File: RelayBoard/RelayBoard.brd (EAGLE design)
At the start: 139.1 x 115.2 mm, 254 parts, among them IC1 MCP2551/SN RSC 402-904, J1 JTAG_ARM_10PIN, J4 JTAG_ARM_10PIN, U1 CD74HC4067SM96, U10 INA219AIDCNR, U11 INA219AIDCNR, U12 INA219AIDCNR, U13 FT230XQ, U14 ADUM1201ARZ, U16 TL1963AKTTR., U2 TL1963AKTTR., U3 CD74HC4067SM96, U4 CD74HC4067SM96, U5 CD74HC4067SM96, U6 TL1963AKTTR., U8 TM4C1294NCPDT, U9 INA219AIDCNR, X1 A1944-50, X2 A1944-50, X3 A1944-50, X4 A1944-50, Y3 NX3225GA, Y4 CRYATL_32K_SMD

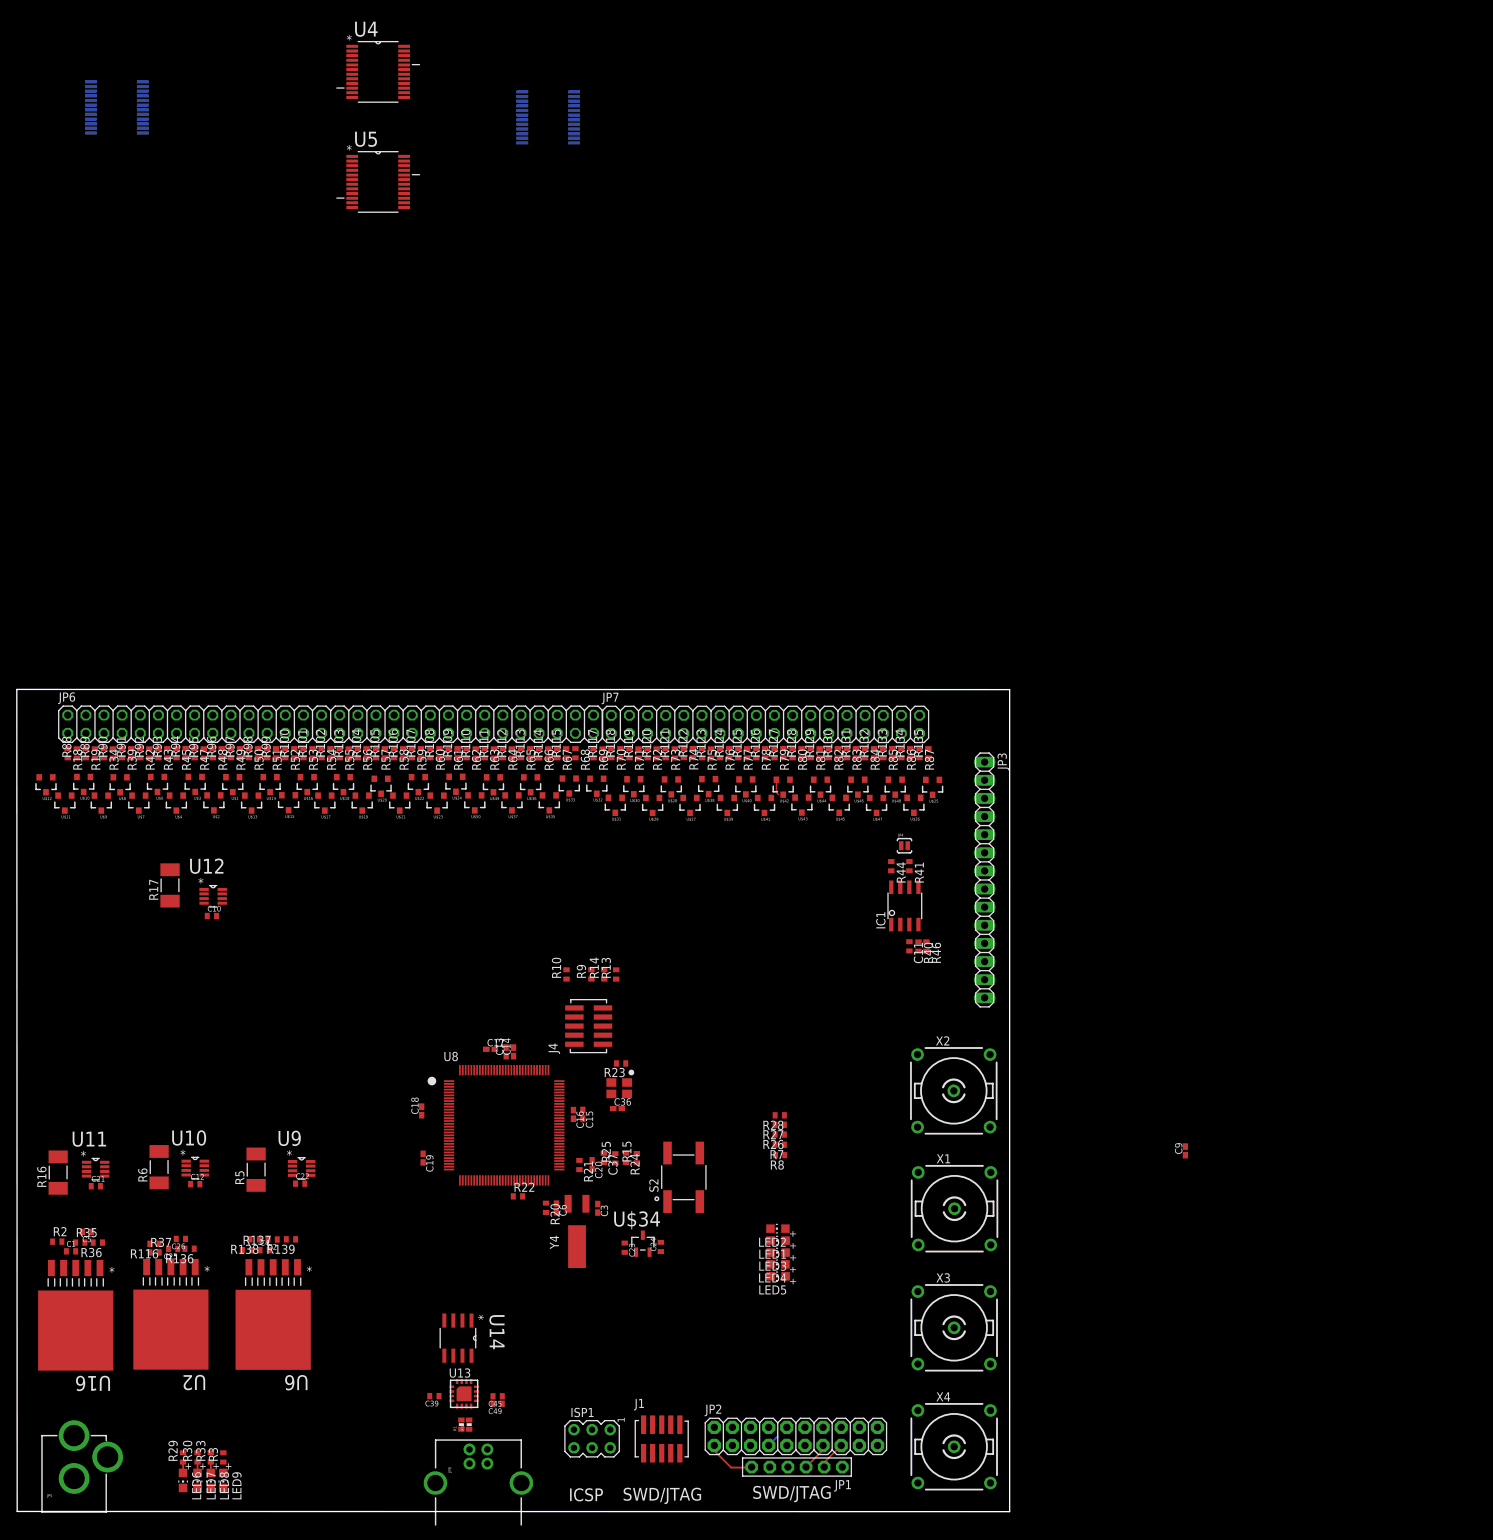
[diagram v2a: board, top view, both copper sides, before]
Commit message: layout done
Add: - binding posts with 19.05 mm spacing
         - top/bottom  VCC/GND plane
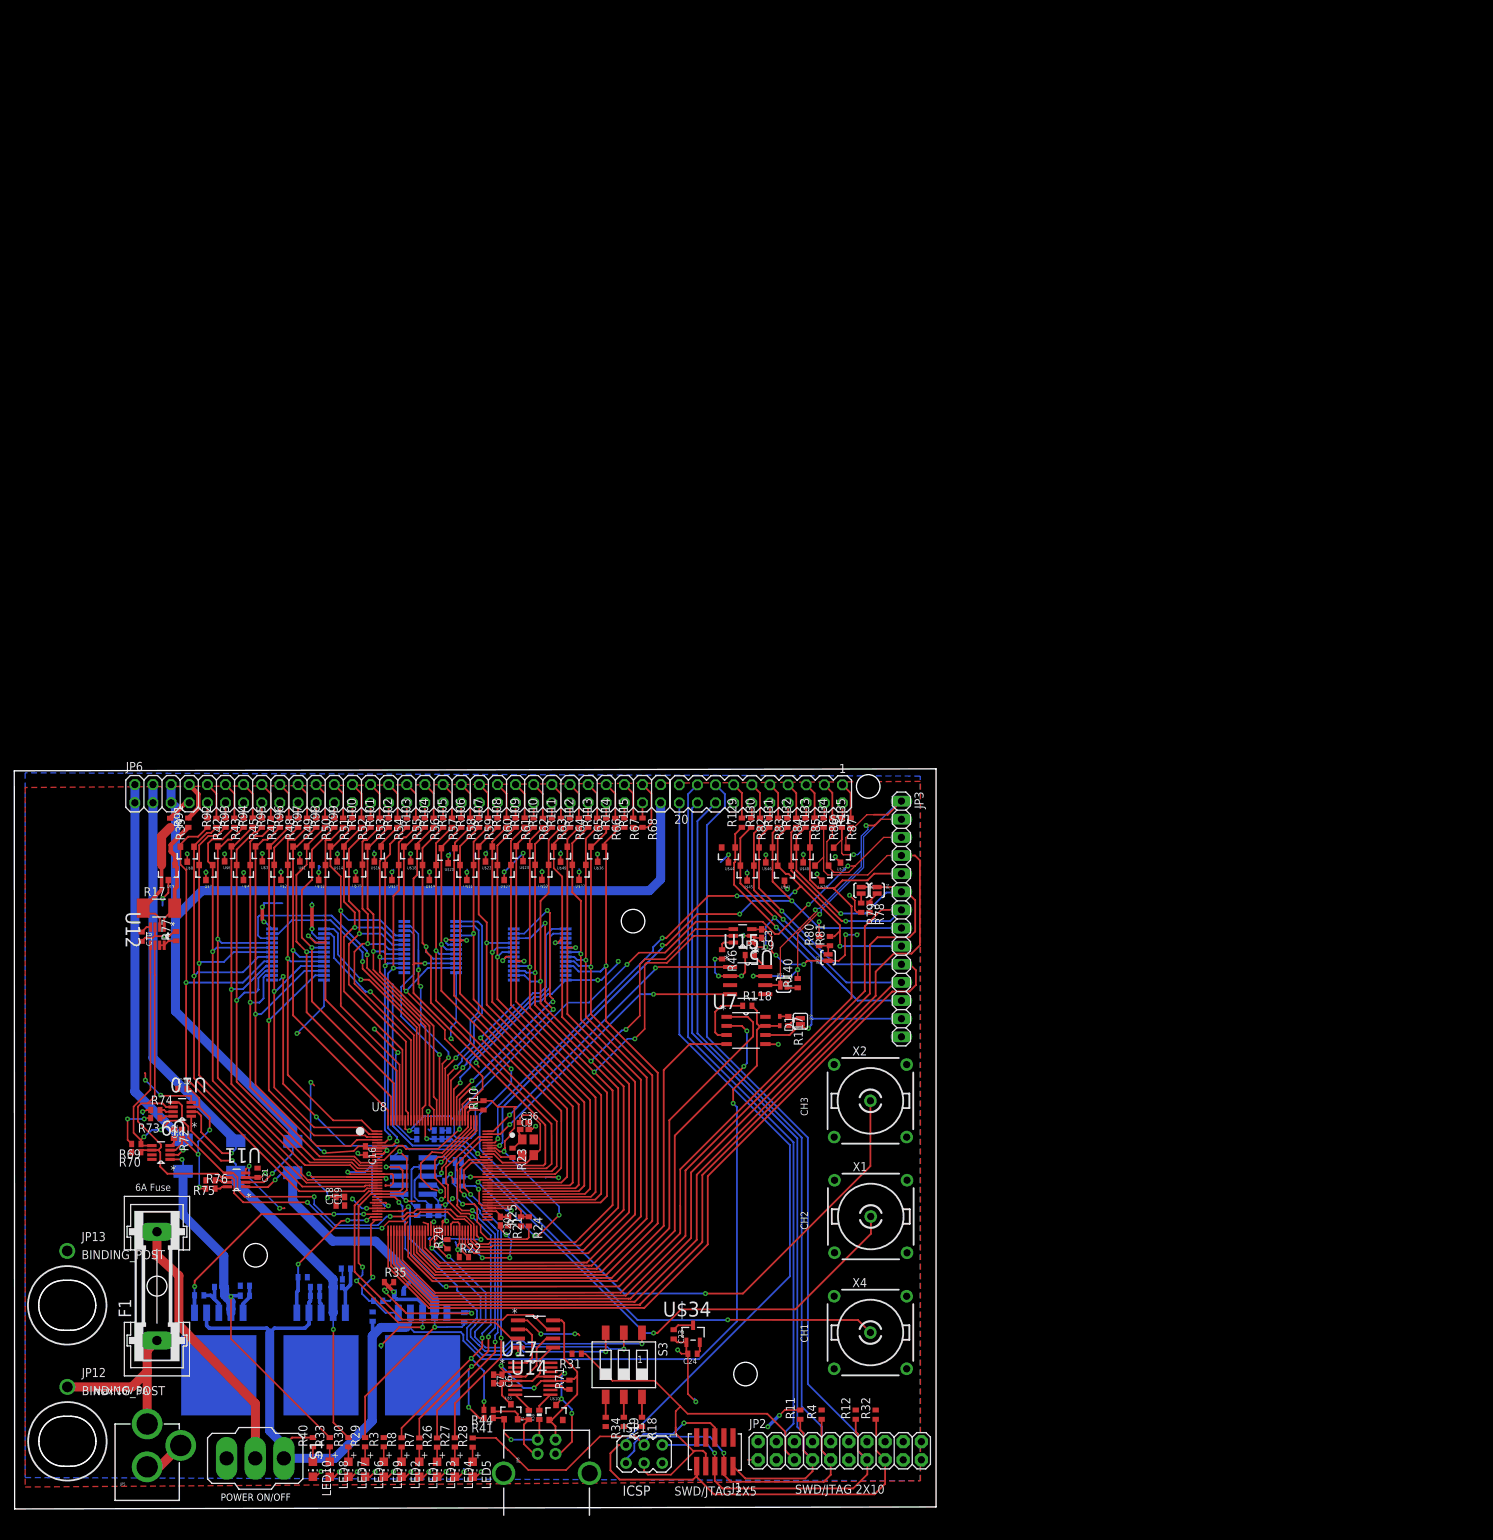
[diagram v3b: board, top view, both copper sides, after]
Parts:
- removed C11: 100nF, eagle-ltspice:C0402
- removed C39, C45: 0.1uF, rcl:C0402
- removed C49: 10uF, rcl:C0402
- removed IC1: MCP2551/SN RSC 402-904, microchip-dspic:SO08
- removed R120, R121, R122, R123, R124, R125, R126, R127, R128, R88, R89, R90: 200R, resistor:R0402
- removed S2: SWITCH_TACTILE, MRDT-UserInput:SWITCH_6MM_6MM_TE_CON_SMD
- removed U$11, U$12, U$27, U$28, U$29, U$30, U$31, U$32, U$33, U$35, U$38, U$39, U$40, U$41, U$42, U$43: zener_3.3V, SparkFun-DiscreteSemi:SOT23-3
- removed U13: FT230XQ, ftdichip:QFN16
- removed X3: A1944-50, con-coax:A1944
- removed Y4: CRYATL_32K_SMD, MRDT-Passives:CRYSTAL_32K_SMD
- added C7: 10uF, rcl:C0402K
- added D1: (no value), diode:SOD523
- added F1: (no value), fuse:GSH15
- added JP10: DUT_CS_MASTER, SparkFun-Retired:SJ_2S-NO
- added JP11: (no value), SparkFun:SJ_2S-NO
- added JP12, JP13: BINDING_POST, SparkFun-Connectors:BINDING_POST
- added JP9: (no value), SparkFun-Retired:SJ_2S
- added LED10: (no value), JDT-1800_smahed:CHIP-LED0805
- added R11, R12, R31, R32, R4: 4k7, resistor:R0402
- added R140: 120, resistor:R0402
- added S1: (no value), switch:320-916
- added S3: SWS003, smd-special:SMS-003
- added STANDOFF1, STANDOFF2, STANDOFF5, STANDOFF6: STAND-OFF, SparkFun-Electromechanical:STAND-OFF
- added SV1: (no value), con-lstb:MA10-2
- added U$5: zener_3.3V, SparkFun-DiscreteSemi:SOT23-3
- added U15: SN65HVD230D, sn65hvd23x:SOIC127P600X175-8N
- added U17: FT230XS, FT230XS:SOP63P600X175-16N
- added U7: MCP2003-E/SN, MCP2003-E_SN:SOIC127P600X175-8N
- C3, C6: value 12pF -> 0.1uF
- JP1: value (none) -> RESET; device JDT-1800_smahed:1X06-BIG -> SparkFun-Retired:SJ_2S-NO
- JP4: value (none) -> DUT_CS_MASTER; device SparkFun:SJ_2S-NO -> SparkFun-Retired:SJ_2S-NO
- JP7: value (none) -> DUT_CS_RecieveAllMSG; device pinhead:2X18 -> SparkFun-Retired:SJ_2S-NO
- R117: value 200R -> 1k
- R118, R119, R72, R73, R74, R75, R76, R77: value 200R -> 4k7
- R136, R139, R36: value (none) -> 4k7
- R18, R19, R34, R69, R70, R71, R78, R79, R80, R81: value 200R -> 4.7k
- R40: value 10k -> (none)
- R41: value 120 -> 0R
- R44: value 4k7 -> 0R
- R46: value 18k -> 4.7k
- U5: value CD74HC4067SM96 -> MCP4725A0T-E/CH; device MUX:SOP65P780X200-24N -> MCP4725:SOT95P270X145-6N
- moved U3 132.6 mm to (73.6, 77.9), turned to 180 degrees
- moved R18 123.5 mm to (87.9, 12.4)
- moved U4 122.8 mm to (58.2, 78.9), flipped to the bottom, turned to 180 degrees
- moved U1 122.4 mm to (39.7, 77.9), turned to 180 degrees
- moved R19 120.2 mm to (85.3, 12.4)
- moved U5 117.3 mm to (102.0, 80.5), turned to 180 degrees
- moved R34 117.1 mm to (82.8, 12.4)
- moved U$10 110.2 mm to (75.8, 13.7), turned to 0 degrees
- moved R40 109.6 mm to (41.8, 9.58), turned to 90 degrees
- moved R41 97.2 mm to (66.4, 13.0), turned to 180 degrees
- moved R44 94.8 mm to (66.4, 14.1), turned to 180 degrees
- moved R76 93.9 mm to (27.4, 45.1), turned to 0 degrees
- moved C9 92.6 mm to (71.4, 53.4), turned to 0 degrees
- moved R75 91.2 mm to (27.4, 46.3), turned to 180 degrees
- moved R74 89.3 mm to (19.7, 56.1), turned to 0 degrees
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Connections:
- removed net 5VSUPPLY: JP2.19
- removed net CAN_N: IC1.6, JP3.2, R41.2
- removed net CAN_P: IC1.7, JP3.1, JP4.1
- removed net CS: JP3.6
- removed net DUT_SH_-: R17.1, U12.2
- removed net EN0LED0: U8.P$42
- removed net EN0LED1: U8.P$46
- removed net EN0RXI_N: U8.P$53
- removed net EN0RXI_P: U8.P$54
- removed net EN0TXO_N: U8.P$56
- removed net EN0TXO_P: U8.P$57
- removed net LIN: JP3.13
- removed net M3S0: U5.10
- removed net M3S1: U5.11
- removed net M3S2: U5.14
- removed net M3S3: U5.13
- removed net MISO: JP3.4
- removed net MOSI: JP3.7
- removed net N$111: JP6.60, R117.2
- removed net N$113: R87.2, U$25.2
- removed net N$114: R88.1, U$12.1
- removed net N$115: R89.1, U$11.1
- removed net N$116: R19.2, U$11.2
- removed net N$117: R90.1, U$10.1
- removed net N$118: R34.2, U$10.2
- removed net N$119: R91.1, U$9.1
- removed net N$120: R39.2, U$9.2
- removed net N$121: R92.1, U$8.1
- removed net N$122: R42.2, U$8.2
- removed net N$123: R43.2, U$7.2
- removed net N$124: R93.1, U$7.1
- removed net N$125: R94.1, U$6.1
- removed net N$126: R45.2, U$6.2
- removed net N$127: R47.2, U$4.2
- removed net N$128: R95.1, U$4.1
- removed net N$129: R96.1, U$3.1
- removed net N$130: R48.2, U$3.2
- removed net N$131: R97.1, U$2.1
- removed net N$132: R49.2, U$2.2
- removed net N$133: R50.2, U$1.2
- removed net N$134: R98.1, U$1.1
- removed net N$135: R99.1, U$13.1
- removed net N$136: R51.2, U$13.2
- removed net N$137: R52.2, U$14.2
- removed net N$138: R100.1, U$14.1
- removed net N$139: R101.1, U$15.1
- removed net N$140: R53.2, U$15.2
- removed net N$141: R54.2, U$16.2
- removed net N$142: R102.1, U$16.1
- removed net N$143: R55.2, U$17.2
- removed net N$144: R103.1, U$17.1
- removed net N$145: R104.1, U$18.1
- removed net N$146: R56.2, U$18.2
- removed net N$147: R105.1, U$19.1
- removed net N$148: R57.2, U$19.2
- removed net N$149: R106.1, U$20.1
- removed net N$150: R58.2, U$20.2
- removed net N$151: R59.2, U$21.2
- removed net N$152: R107.1, U$21.1
- removed net N$157: R135.1, U$25.1
- removed net N$159: C39.2, U13.8
- removed net N$160: R134.1, U$26.1
- removed net N$161: R86.2, U$26.2
- removed net N$162: R85.2, U$48.2
- removed net N$163: R133.1, U$48.1
- removed net N$164: R84.2, U$47.2
- removed net N$165: R83.2, U$46.2
- removed net N$166: R82.2, U$45.2
- removed net N$167: R81.2, U$44.2
- removed net N$168: R80.2, U$43.2
- removed net N$169: R79.2, U$42.2
- removed net N$170: R78.2, U$41.2
- removed net N$171: R77.2, U$40.2
- removed net N$172: R76.2, U$39.2
- removed net N$173: R75.2, U$38.2
- removed net N$174: R73.2, U$28.2
- removed net N$175: R72.2, U$29.2
- removed net N$176: R71.2, U$30.2
- removed net N$177: R70.2, U$31.2
- removed net N$178: R69.2, U$32.2
- removed net N$179: R68.2, U$33.1
- removed net N$181: R66.2, U$36.2
- removed net N$182: R129.1, U$44.1
- removed net N$183: R132.1, U$47.1
- removed net N$184: R131.1, U$46.1
- removed net N$185: R130.1, U$45.1
- removed net N$186: R74.2, U$27.2
- removed net N$187: R128.1, U$43.1
- removed net N$188: R127.1, U$42.1
- removed net N$189: R65.2, U$37.2
- removed net N$190: R64.2, U$49.2
- removed net N$191: R63.2, U$50.2
- removed net N$192: R126.1, U$41.1
- removed net N$193: R125.1, U$40.1
- removed net N$194: R124.1, U$39.1
- removed net N$195: R123.1, U$38.1
- removed net N$196: R122.1, U$27.1
- removed net N$197: R121.1, U$28.1
- removed net N$198: R120.1, U$29.1
- removed net N$199: R119.1, U$30.1
- removed net N$200: R118.1, U$31.1
- removed net N$201: R117.1, U$32.1
- removed net N$203: R115.1, U$33.2
- removed net N$204: R114.1, U$36.1
- removed net N$205: R113.1, U$37.1
- removed net N$206: R112.1, U$49.1
- removed net N$207: R111.1, U$50.1
- removed net N$53: JP7.15, R77.1
- removed net N$54: JP7.17, R78.1
- removed net N$55: JP7.19, R79.1
- removed net N$56: JP7.21, R80.1
- removed net N$57: JP7.23, R81.1
- removed net N$63: JP7.35, R87.1
- removed net N$66: JP7.6, R120.2
- removed net N$67: JP7.8, R121.2
- removed net N$68: JP7.10, R122.2
- removed net N$69: JP7.12, R123.2
- removed net N$70: JP7.14, R124.2
- removed net N$71: JP7.16, R125.2
- removed net N$72: JP7.18, R126.2
- removed net N$73: JP7.20, R127.2
- removed net N$74: JP7.22, R128.2
- removed net N$81: JP7.36, R135.2
- removed net N$82: JP6.2, R88.2
- removed net N$83: JP6.4, R89.2
- removed net N$84: JP6.6, R90.2
- removed net N_$34: C6.1, U8.P$66, Y4.P$1
- removed net N_$35: C3.1, U8.P$67, Y4.P$2
- removed net ONEWIRE: JP3.3
- removed net PI_5V: C11.1, IC1.3
- removed net POWER_IN: C25.1, C26.1, C5.1, JP5.PWR, U16.2, U2.2, U6.2
- removed net PROGRAM: R28.2
- removed net SCL: JP3.9
- removed net SCLK: JP3.5
- removed net SDA: JP3.8
- removed net SWDCLK: JP1.4
- removed net SWDIO: JP1.5
- removed net SWO: JP1.3
- removed net SWO/TDO/MISO: ISP1.1, J1.P6, JP2.13
- removed net TDI/MOSI: ISP1.4, J1.P8
- removed net TRST_3V3: R136.2, R139.2, R36.2
- new net AD0: R42.2, U$8.2, U1.5, U8.P$21
- new net AD1: R92.1, U$8.1, U1.6, U8.P$20
- new net AD10: R49.2, U$2.2, U1.21, U8.P$2
- new net AD11: R97.1, U$2.1, U1.20, U8.P$1
- new net AD12: R50.2, U$1.2, U1.19, U8.P$128
- new net AD13: R98.1, U$1.1, U1.18, U8.P$127
- new net AD14: R51.2, U$13.2, U1.17, U8.P$126
- new net AD15: R99.1, U$13.1, U1.16, U8.P$125
- new net AD16: R52.2, U$14.2, U4.9, U8.P$124
- new net AD17: R100.1, U$14.1, U4.8, U8.P$123
- new net AD18: R53.2, U$15.2, U4.7, U8.P$121
- new net AD19: R101.1, U$15.1, U4.6, U8.P$120
- new net AD2: R43.2, U$7.2, U1.7, U8.P$19
- new net AD3: R93.1, U$7.1, U1.8, U8.P$18
- new net AD4: R45.2, U$6.2, U1.9, U8.P$15
- new net AD5: R94.1, U$6.1, U1.4, U8.P$14
- new net AD6: R47.2, U$4.2, U1.3, U8.P$13
- new net AD7: R95.1, U$4.1, U1.2, U8.P$12
- new net AD8: R48.2, U$3.2, U1.22, U8.P$4
- new net AD9: R96.1, U$3.1, U1.23, U8.P$3
- new net CAN_RX: U15.4, U8.P$95
- new net CAN_TX: U15.1, U8.P$96
- new net CH1: U4.1
- new net CH2: U1.1
- new net CH3: U3.1
- new net D0: R54.2, U$16.2, U4.5, U8.P$112
- new net D1: R102.1, U$16.1, U4.4, U8.P$111
- new net D10: R59.2, U$21.2, U4.17, U8.P$77
- new net D11: R107.1, U$21.1, U4.16, U8.P$76
- new net D12: R60.2, U$22.2, U3.9, U8.P$75
- new net D13: R108.1, U$22.1, U3.8, U8.P$74
- new net D14: R61.2, U$23.2, U3.7, U8.P$73
- new net D15: R109.1, U$23.1, U3.6, U8.P$72
- new net D16: R62.2, U$24.2, U3.5, U8.P$71
- new net D19: R111.1, U$50.1, U3.2, U8.P$61
- new net D2: R55.2, U$17.2, U4.3, U8.P$5
- new net D20: R64.2, U$49.2, U3.16, U8.P$60
- new net D21: R112.1, U$49.1, U3.17, U8.P$46
- new net D22: R65.2, U$37.2, U3.18, U8.P$45
- new net D23: R113.1, U$37.1, U3.19, U8.P$44
- new net D24: R66.2, U$36.2, U3.20, U8.P$43
- new net D25: R114.1, U$36.1, U3.21, U8.P$42
- new net D26: U3.22
- new net D27: U3.23
- new net D3: R103.1, U$17.1, U4.2, U8.P$6
- new net D4: R56.2, U$18.2, U4.23, U8.P$102
- new net D5: R104.1, U$18.1, U4.22, U8.P$84
- new net D6: R57.2, U$19.2, U4.21, U8.P$83
- new net D7: R105.1, U$19.1, U4.20, U8.P$82
- new net D8: R58.2, U$20.2, U4.19, U8.P$81
- new net D9: R106.1, U$20.1, U4.18, U8.P$78
- new net DUT_AOUT1: JP3.12, R82.2, U$45.2, U5.1
- new net DUT_CAN_N: JP11.1, JP3.2, R87.2, U$25.2, U15.6
- new net DUT_CAN_P: JP3.1, R135.1, R140.2, U$25.1, U15.7
- new net DUT_CS: JP3.6, JP4.1, JP7.1, R85.2, U$48.2, U8.P$36
- new net DUT_LIN: JP3.13, JP9.2, R129.1, U$44.1, U7.6
- new net DUT_MISO: JP3.4, R86.2, U$26.2, U8.P$35
- new net DUT_MOSI: JP3.7, R132.1, U$47.1, U8.P$37
- new net DUT_ONEWIRE: JP3.3, R134.1, U$26.1, U8.P$11
- new net DUT_RX: JP3.10, R83.2, U$46.2, U8.P$33
- new net DUT_SCL: JP3.8, R131.1, R80.2, U$46.1, U8.P$91
- new net DUT_SCLK: JP3.5, R133.1, U$48.1, U8.P$38
- new net DUT_SDA: JP3.9, R81.2, R84.2, U$47.2, U8.P$92
- new net DUT_SH-: R17.1, R39.2, U$9.2, U12.2
- new net DUT_TX: JP3.11, R130.1, U$45.1, U8.P$34
- new net LIN_CS: U7.2, U8.P$24
- new net LIN_RX: U7.1, U8.P$40
- new net LIN_TX: U7.4, U8.P$41
- new net M0OUT: X4.1
- new net N$153: LED10.A, R40.1
- new net PC4: U8.P$25
- new net POWER_IN_12V: C25.1, C26.1, C5.1, D1.A, R118.2, R40.2, S1.1, U16.2, U2.2, U6.2, U7.7
- new net SW1: S3.3, U8.P$29
- new net SW2: S3.2, U8.P$49
- new net SW3: S3.1, U8.P$50
- new net SWO/TDO/MOSI: ISP1.1, J1.P6, JP2.13, R12.1, SV1.15
- new net TSTR_SCL1: JP4.2, R78.1
- new net VREN: U7.8
- net !RESET: now also JP1.2; no longer S2.P$3, S2.P$4
- net DUT_CONNECT: now also U8.P$85
- net DUT_SH+: now also R91.1, U$9.1
- net GND: now also JP13.P$1, JP6.58, JP6.60, LED10.C, R115.1, R119.1, R136.2, R139.2, R36.2, R46.2, R68.2, R74.1, R76.1, R77.2, R79.2, U15.2, U5.2, U7.5; no longer C11.2, C6.2, IC1.2, R44.1, R46.1, S2.P$1, S2.P$2, U$10.3, U$11.3, U$12.3, U$27.3, U$28.3, U$29.3, U$30.3, U$31.3, U$32.3, U$33.3, U$35.3, U$38.3, U$39.3, U$40.3, U$41.3, U$42.3, U$43.3, U10.7, U11.8, U12.7, U12.8, U5.12, U5.15, X3.2, X3.3, X3.4, X3.5
- net HOST_GND: now also C6.2, C7.2, JP8.GND, U$10.3, U$5.3, U17.13, U17.5; no longer C39.1, C45.1, C49.1, U13.13, U13.3
- net HOST_UART_RX: now also U17.4; no longer U13.2
- net HOST_UART_TX: now also U17.1; no longer U13.15
- net LDO1: now also JP6.5, JP6.59, JP6.6; no longer R108.1, R29.2, R60.2, U$22.1, U$22.2
- net LDO1_ENABLE: now also U8.P$32
- net LDO1_SH+: now also R29.2
- net LDO2: now also JP6.3, JP6.4; no longer R109.1, R30.2, R61.2, U$23.1, U$23.2
- net LDO2_ENABLE: now also U8.P$31
- net LDO2_SH+: now also R30.2
- net LDO3: now also JP6.1, JP6.2; no longer R110.1, R33.2, R62.2, U$24.1, U$24.2
- net LDO3_ENABLE: now also U8.P$30
- net LDO3_SH+: now also R33.2
- net M0S0: now also U4.13, U8.P$107; no longer U4.10
- net M0S1: now also U4.14, U8.P$108; no longer U4.11
- net M0S2: now also U4.11, U8.P$109; no longer U4.14
- net M0S3: now also U4.10, U8.P$110; no longer U4.13
- net M1OUT: no longer U1.1, U4.1
- net M1S0: now also U8.P$116
- net M1S1: now also U8.P$117
- net M1S2: now also U8.P$119
- net M1S3: now also U8.P$118
- net M2OUT: no longer U3.1, U5.1
- net M2S0: now also U8.P$103
- net M2S1: now also U8.P$104
- net M2S2: now also U8.P$105
- net M2S3: now also U8.P$106
- net N$1: now also R46.1, U5.6; no longer JP3.12
- net N$112: now also R119.2, U15.8; no longer R18.2, U$12.2
- net N$180: no longer U$35.2
- net N$2: now also JP11.2, R140.1; no longer R10.2, R13.2, R14.2, R15.2, R9.2
- net N$4: now also R87.1, SV1.2; no longer JP6.1, R18.1
- net N$40: now also F1.1, JP12.P$1, JP5.PWR; no longer JP6.59, R69.1
- net N$41: now also R18.1, S3.6; no longer JP7.1, R70.1
- net N$42: now also R19.1, S3.5; no longer JP7.3, R71.1
- net N$43: now also R34.1, S3.4; no longer JP7.5, R72.1
- net N$44: now also R71.1, U17.11; no longer JP4.2, R41.1
- net N$45: now also R73.1, U10.8; no longer R40.2, R46.2
- net N$46: now also R75.1, U11.7; no longer IC1.4, R40.1
- net N$47: now also D1.C, R117.1; no longer IC1.1
- net N$48: now also R74.2, U10.7; no longer IC1.8, R44.2
- net N$49: now also JP7.2, R79.1; no longer JP7.7, R73.1
- net N$50: now also R76.2, U11.8; no longer JP7.9, R74.1
- net N$51: now also R77.1, U12.7, U12.8; no longer JP7.11, R75.1
- net N$52: now also JP10.2, R80.1, R81.1; no longer JP7.13, R76.1
- net N$58: now also SV1.12; no longer JP7.25
- net N$59: now also SV1.10; no longer JP7.27
- net N$6: now also R135.2, SV1.1; no longer JP6.3, R19.1
- net N$60: now also SV1.8; no longer JP7.29
- net N$61: now also SV1.6; no longer JP7.31
- net N$62: now also SV1.4; no longer JP7.33
- net N$64: now also R118.1, U7.3; no longer JP7.2, R118.2
- net N$65: now also JP9.1, R117.2; no longer JP7.4, R119.2
- net N$7: now also F1.2, S1.2; no longer JP6.5, R34.1
- net N$75: now also SV1.13; no longer JP7.24
- net N$76: now also SV1.11; no longer JP7.26
- net N$77: now also SV1.9; no longer JP7.28
- net N$78: now also SV1.7; no longer JP7.30
- net N$79: now also SV1.5; no longer JP7.32
- net N$80: now also SV1.3; no longer JP7.34
- net NRESET: now also R32.1, SV1.20; no longer JP1.2
- net SWDCLK/TCLK/SCK: now also R28.2, R4.1, SV1.16
- net SWDIO/TMS: now also R11.1, SV1.18
- net TDI/MISO: now also ISP1.4, J1.P8, R31.1, SV1.17
- net TEST_FAIL: now also U8.P$86
- net TEST_PASS: now also R41.2, U8.P$93
- net TEST_RUN: now also R44.2, U8.P$94
- net TSTR_3V3: now also C3.1, JP10.1, JP2.1, R10.2, R11.2, R12.2, R13.2, R14.2, R15.2, R18.2, R19.2, R31.2, R32.2, R34.2, R4.2, R69.2, R70.2, R72.1, R73.2, R75.2, R78.2, R9.2, U1.24, U15.3, U3.24, U4.24, U5.3; no longer U10.8, U11.7, U9.4
- net TSTR_RX: now also U8.P$22; no longer JP3.10, U8.P$33
- net TSTR_SCL: now also R110.1, R69.1, U$24.1, U3.4, U5.5, U8.P$63
- net TSTR_SDA: now also R63.2, R70.1, U$50.2, U3.3, U5.4, U8.P$62
- net TSTR_TX: now also U8.P$23; no longer JP3.11, U8.P$34
- net USBD_N: now also U17.9; no longer U13.7
- net USBD_P: now also U17.8; no longer U13.6
- net USB_N: now also R41.1, U$5.1
- net USB_P: now also R44.1, U$5.2
- net VBUS: now also C6.1, C7.1, R71.2, U$10.1, U17.12, U17.3; no longer C45.2, C49.2, U13.1, U13.10
- net VCC: now also R72.2, U9.4; no longer JP1.6, JP2.1, U1.24, U3.24, U4.24, U5.24
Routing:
- net GND: track 0.00 -> 310.9 mm, vias 0 -> 79
- net TSTR_3V3: track 0.00 -> 273.0 mm, vias 0 -> 38
- net TSTR_SCL: track 0.00 -> 210.1 mm, vias 0 -> 7
- net TSTR_SDA: track 0.00 -> 209.8 mm, vias 0 -> 5
- net POWER_IN_12V: track 0.00 -> 184.9 mm, vias 0 -> 1
- net SWDCLK/TCLK/SCK: track 0.00 -> 169.2 mm, vias 0 -> 1
- net TDI/MISO: track 0.00 -> 161.3 mm
- net NRESET: track 4.01 -> 162.9 mm
- net DUT_CS: track 0.00 -> 149.9 mm, vias 0 -> 1
- net SWO/TDO/MOSI: track 0.00 -> 148.2 mm, vias 0 -> 1
- net LDO1: track 0.00 -> 147.9 mm, vias 0 -> 1
- net DUT_RX: track 0.00 -> 143.7 mm, vias 0 -> 1
- net DUT_MISO: track 0.00 -> 143.4 mm
- net DUT_TX: track 0.00 -> 138.1 mm, vias 0 -> 1
- net DUT_MOSI: track 0.00 -> 135.1 mm, vias 0 -> 1
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- added copper zone on layer 16, net GND
- added copper zone on layer 1, net TSTR_3V3
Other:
- board size 139.1 x 115.2 mm -> 129.1 x 103.7 mm
- board text added: "6A Fuse"
- board text added: "CH1"
- board text added: "CH2"
- board text added: "CH3"
- board text added: "DUT CON"
- board text added: "LDO1"
- board text added: "LDO2"
- board text added: "LDO3"
- board text added: "POWER ON/OFF"
- board text added: "PROGRAM"
- board text added: "PWR_IN"
- board text added: "SWD/JTAG 2X10"
- board text added: "SWD/JTAG 2X5"
- board text added: "TEST FAIL"
- board text added: "TEST PASS"
- board text added: "TEST RUN"
- board text added: "TSTR_3V3"
- board text added: "max 16V 5A"
- board text removed: "SWD/JTAG"

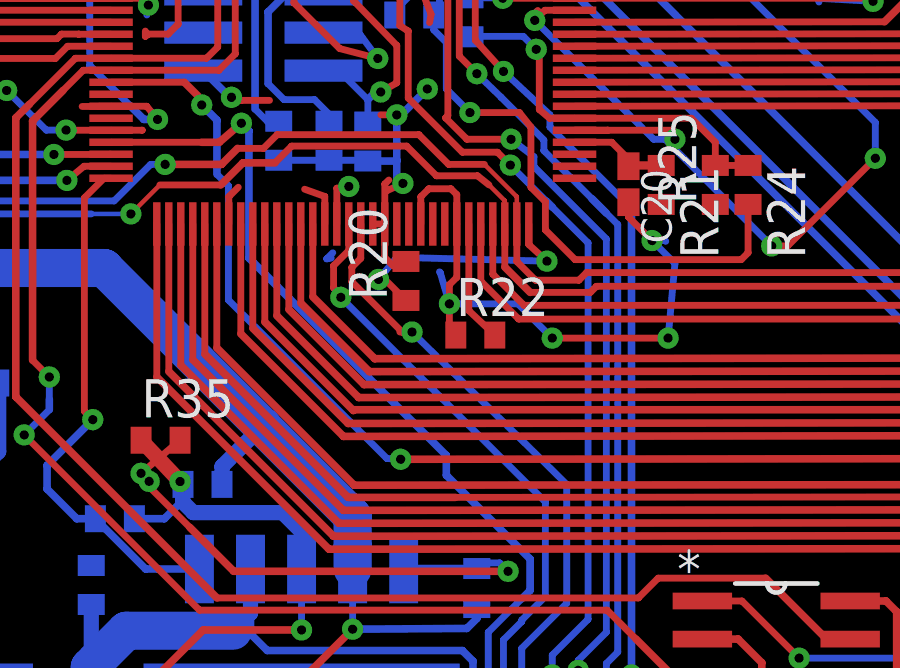
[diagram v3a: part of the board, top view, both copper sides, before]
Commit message: fix - close cap to mcu
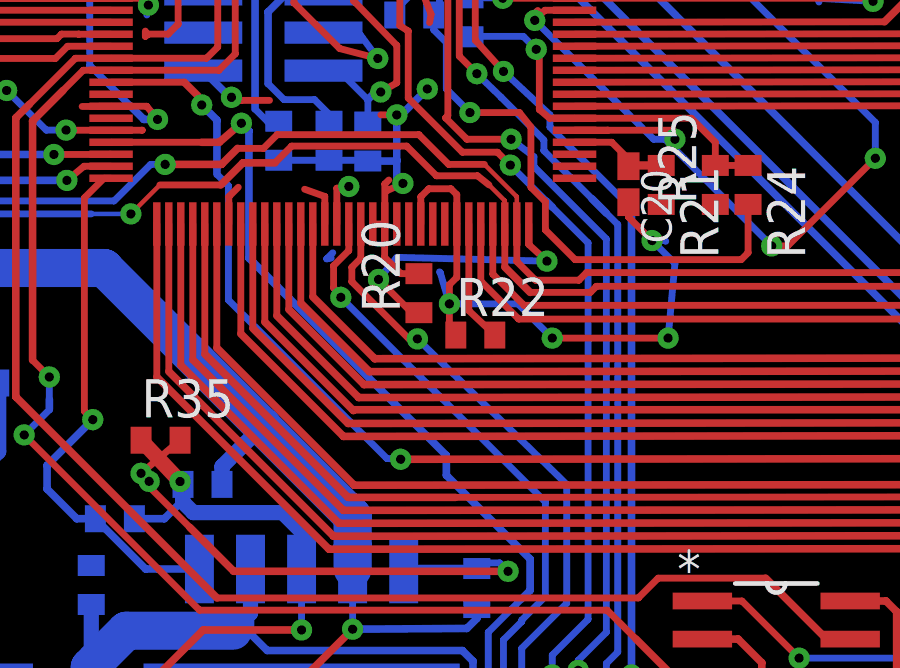
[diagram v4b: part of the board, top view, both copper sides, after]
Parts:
- moved R20 0.59 mm to (61.1, 36.9)
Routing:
- net N_$24: track 8.67 -> 9.27 mm
- net TSTR_3V3: track 273.0 -> 273.5 mm
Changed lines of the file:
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@@
 <element name="JP6" library="pinhead" package="2X30" value="" x="54.9402" y="100.4316"/>
 <element name="U8" library="MRDT-Microcontrollers" package="TQFP-128" value="TM4C1294NCPDT" x="50.8" y="53.1368"/>
-<element name="R20" library="rcl" package="R0402" value="1M" x="60.6298" y="37.3126" rot="R90"/>
+<element name="R20" library="rcl" package="R0402" value="1M" x="61.0616" y="36.9062" rot="R90"/>
 <element name="R21" library="rcl" package="R0402" value="51" x="69.1388" y="40.513" rot="R270"/>
 <element name="R22" library="rcl" package="R0402" value="4.87k 1%" x="62.9412" y="35.5092"/>
@@
 <contactref element="U8" pad="P$64"/>
 <contactref element="R20" pad="1"/>
-<wire x1="60.6298" y1="36.6626" x2="59.929" y2="37.3634" width="0.2286" layer="1"/>
-<wire x1="59.929" y1="37.3634" x2="59.7154" y2="37.3634" width="0.2286" layer="1"/>
+<wire x1="59.929" y1="37.3634" x2="59.7154" y2="37.3634" width="0" layer="19" extent="1-16"/>
 <via x="59.7154" y="37.3634" extent="1-16" drill="0.3048"/>
 <wire x1="59.7154" y1="37.3634" x2="60.325" y2="38.1" width="0.2286" layer="16"/>
@@
 <wire x1="65.3288" y1="37.973" x2="64.725" y2="38.526" width="0.2286" layer="1"/>
 <wire x1="64.725" y1="38.526" x2="64.725" y2="39.2118" width="0.2286" layer="1"/>
+<wire x1="61.0616" y1="36.2562" x2="60.8226" y2="36.2562" width="0.2286" layer="1"/>
+<wire x1="60.8226" y1="36.2562" x2="59.7154" y2="37.3634" width="0.2286" layer="1"/>
 </signal>
 <signal name="N_$28">
@@
 <wire x1="65.4916" y1="57.2262" x2="65.6844" y2="57.419" width="0.2286" layer="1"/>
 <wire x1="59.925" y1="39.2118" x2="59.525" y2="39.2118" width="0.2286" layer="1"/>
-<wire x1="60.6298" y1="37.9626" x2="60.183" y2="37.8356" width="0.2286" layer="1"/>
-<wire x1="60.183" y1="37.8356" x2="59.9186" y2="38.1" width="0.2286" layer="1"/>
 <wire x1="59.9186" y1="38.1" x2="59.9186" y2="39.2054" width="0.2286" layer="1"/>
 <wire x1="59.9186" y1="39.2054" x2="59.925" y2="39.2118" width="0.2286" layer="1"/>
@@
 <wire x1="32.8168" y1="46.6598" x2="32.8168" y2="48.2092" width="0.254" layer="16"/>
 <wire x1="32.8168" y1="48.2092" x2="32.8676" y2="48.26" width="0.254" layer="16"/>
+<wire x1="61.0616" y1="37.5562" x2="60.4624" y2="37.5562" width="0.2286" layer="1"/>
+<wire x1="60.4624" y1="37.5562" x2="59.9186" y2="38.1" width="0.2286" layer="1"/>
 </signal>
 <signal name="LDO1_SH+" class="5">
@@
 <wire x1="64.4906" y1="25.0698" x2="65.9892" y2="26.5684" width="0.2286" layer="16"/>
 <wire x1="65.9892" y1="26.5684" x2="65.9892" y2="30.5308" width="0.2286" layer="16"/>
-<wire x1="65.9892" y1="30.5308" x2="60.833" y2="35.6108" width="0.2286" layer="16"/>
-<via x="60.833" y="35.6108" extent="1-16" drill="0.3048" diameter="0.3048"/>
-<wire x1="60.4266" y1="35.6108" x2="60.833" y2="35.6108" width="0.2286" layer="1"/>
+<wire x1="65.9892" y1="30.5308" x2="61.0108" y2="35.3822" width="0.2286" layer="16"/>
+<via x="61.0108" y="35.3822" extent="1-16" drill="0.3048" diameter="0.3048"/>
 <wire x1="59.125" y1="39.2118" x2="59.125" y2="38.0684" width="0.2286" layer="1"/>
 <wire x1="59.125" y1="38.0684" x2="58.8264" y2="37.7698" width="0.2286" layer="1"/>
 <wire x1="58.8264" y1="37.7698" x2="58.8264" y2="37.2872" width="0.2286" layer="1"/>
-<wire x1="58.8264" y1="37.2872" x2="60.5028" y2="35.6108" width="0.2286" layer="1"/>
-<wire x1="60.5028" y1="35.6108" x2="60.833" y2="35.6108" width="0.2286" layer="1"/>
+<wire x1="58.8264" y1="37.2872" x2="60.7314" y2="35.3822" width="0.2286" layer="1"/>
+<wire x1="61.0108" y1="35.3822" x2="60.7314" y2="35.3822" width="0.2286" layer="1"/>
 </signal>
 <signal name="DUT_AOUT1">
